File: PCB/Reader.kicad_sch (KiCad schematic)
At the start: 42 parts, among them J1 Conn_01x04, J2 Amphenol Dubox ‎76383-402LF‎, J3 Conn_01x04, J4 Conn_01x08, J5 Conn_01x10, J6 Conn_01x03, J7 Conn_01x02, Q1 2N7002, Q2 2N7002, Q3 2N7002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

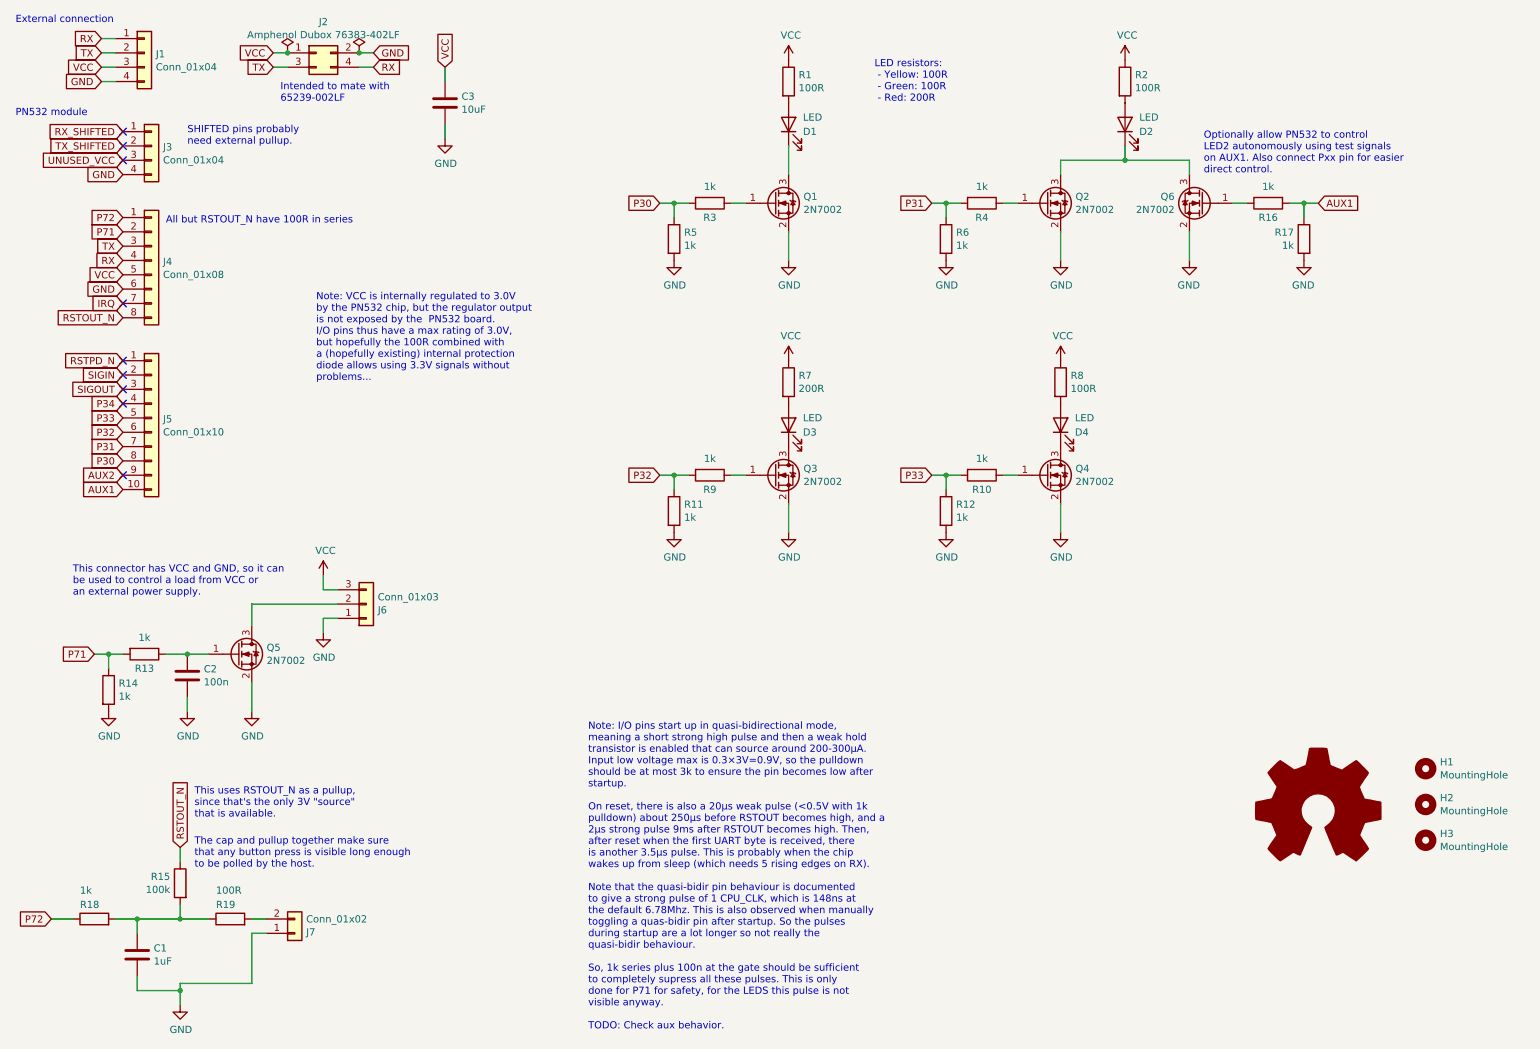
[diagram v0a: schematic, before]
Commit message: Improve some schematic notes
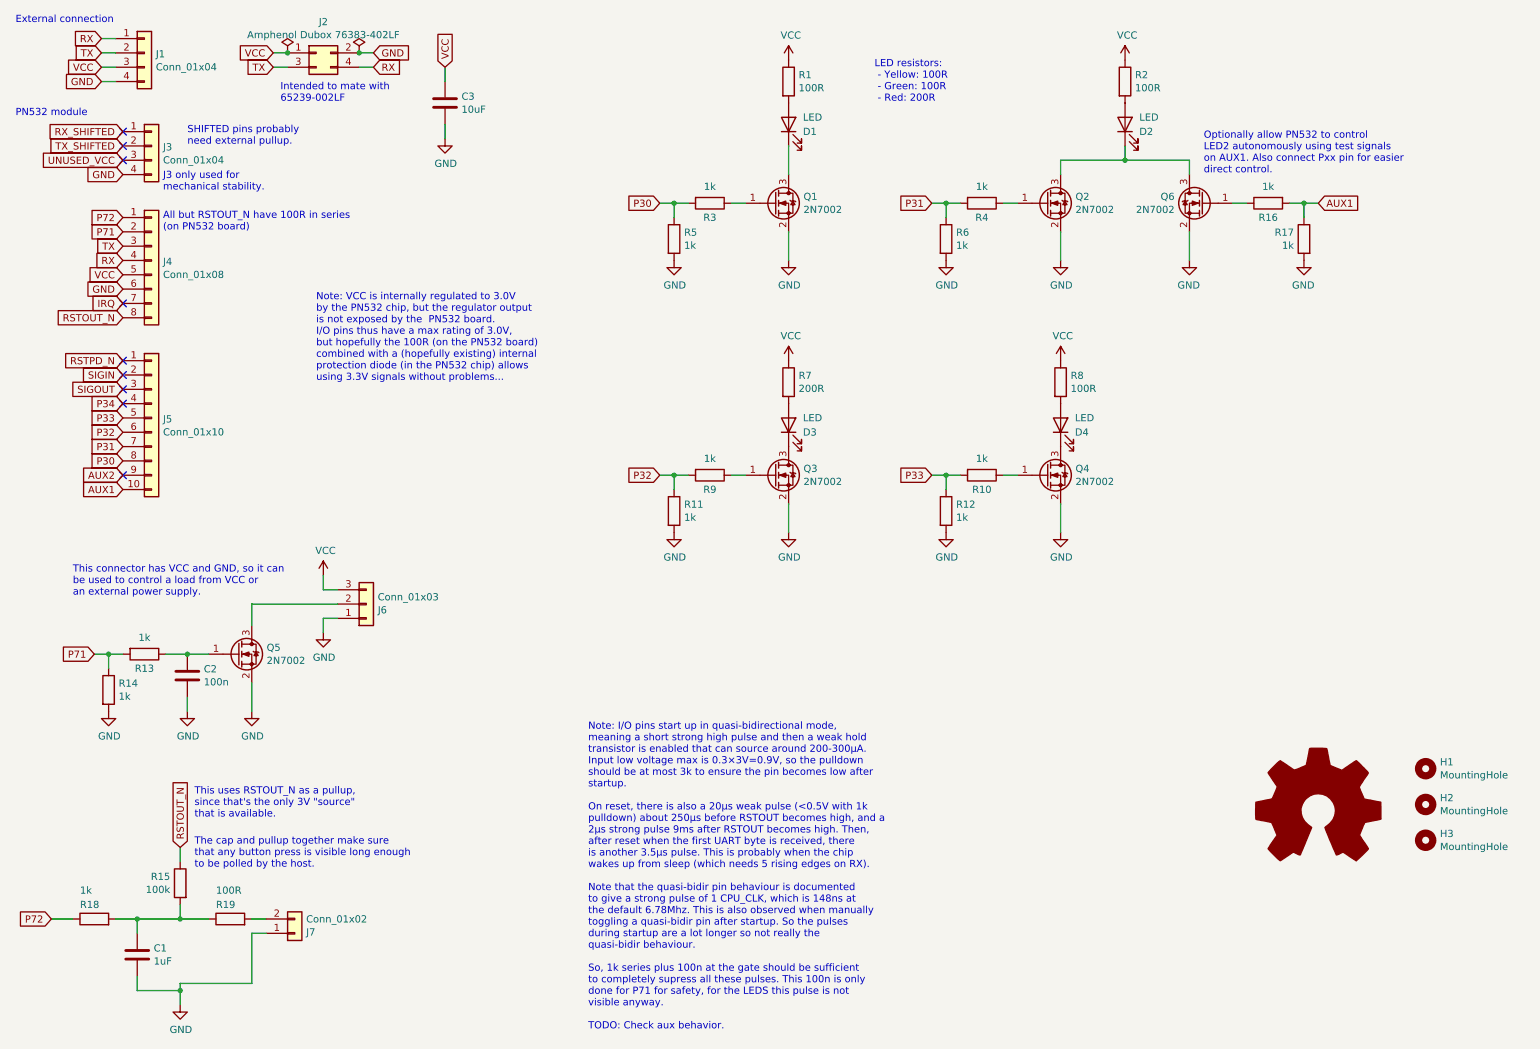
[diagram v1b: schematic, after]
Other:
- note added: "All but RSTOUT_N have 100R in series (on PN532 board)"
- note added: "J3 only used for mechanical stability."
- note added: "Note: VCC is internally regulated to 3.0V by the PN532 chip, but the regulator output is not exposed by the PN532 board. I/O pins thus have a max rating of 3.0V, but hopefully the 100R (on the PN532 board) combined with a (hopefully existing) internal protection diode (in the PN532 chip) allows using 3.3V signals without problems..."
- note removed: "All but RSTOUT_N have 100R in series"
- note removed: "Note: VCC is internally regulated to 3.0V by the PN532 chip, but the regulator output is not exposed by the PN532 board. I/O pins thus have a max rating of 3.0V, but hopefully the 100R combined with a (hopefully existing) internal protection diode allows using 3.3V signals without problems..."
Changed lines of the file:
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@@
 		)
 	)
-	(text "Note: VCC is internally regulated to 3.0V\nby the PN532 chip, but the regulator output\nis not exposed by the  PN532 board.\nI/O pins thus have a max rating of 3.0V,\nbut hopefully the 100R combined with\na (hopefully existing) internal protection\ndiode allows using 3.3V signals without\nproblems..."
+	(text "Note: VCC is internally regulated to 3.0V\nby the PN532 chip, but the regulator output\nis not exposed by the  PN532 board.\nI/O pins thus have a max rating of 3.0V,\nbut hopefully the 100R (on the PN532 board)\ncombined with a (hopefully existing) internal\nprotection diode (in the PN532 chip) allows\nusing 3.3V signals without problems..."
 		(exclude_from_sim no)
 		(at 68.58 78.74 0)
@@
 		)
 	)
-	(text "Note: I/O pins start up in quasi-bidirectional mode,\nmeaning a short strong high pulse and then a weak hold\ntransistor is enabled that can source around 200-300μA.\nInput low voltage max is 0.3×3V=0.9V, so the pulldown\nshould be at most 3k to ensure the pin becomes low after\nstartup.\n\nOn reset, there is also a 20μs weak pulse (<0.5V with 1k\npulldown) about 250μs before RSTOUT becomes high, and a\n2μs strong pulse 9ms after RSTOUT becomes high. Then,\nafter reset when the first UART byte is received, there\nis another 3.5μs pulse. This is probably when the chip\nwakes up from sleep (which needs 5 rising edges on RX).\n\nNote that the quasi-bidir pin behaviour is documented\nto give a strong pulse of 1 CPU_CLK, which is 148ns at\nthe default 6.78Mhz. This is also observed when manually\ntoggling a quas-bidir pin after startup. So the pulses\nduring startup are a lot longer so not really the\nquasi-bidir behaviour.\n\nSo, 1k series plus 100n at the gate should be sufficient\nto completely supress all these pulses. This is only\ndone for P71 for safety, for the LEDS this pulse is not\nvisible anyway.\n\nTODO: Check aux behavior."
+	(text "Note: I/O pins start up in quasi-bidirectional mode,\nmeaning a short strong high pulse and then a weak hold\ntransistor is enabled that can source around 200-300μA.\nInput low voltage max is 0.3×3V=0.9V, so the pulldown\nshould be at most 3k to ensure the pin becomes low after\nstartup.\n\nOn reset, there is also a 20μs weak pulse (<0.5V with 1k\npulldown) about 250μs before RSTOUT becomes high, and a\n2μs strong pulse 9ms after RSTOUT becomes high. Then,\nafter reset when the first UART byte is received, there\nis another 3.5μs pulse. This is probably when the chip\nwakes up from sleep (which needs 5 rising edges on RX).\n\nNote that the quasi-bidir pin behaviour is documented\nto give a strong pulse of 1 CPU_CLK, which is 148ns at\nthe default 6.78Mhz. This is also observed when manually\ntoggling a quasi-bidir pin after startup. So the pulses\nduring startup are a lot longer so not really the\nquasi-bidir behaviour.\n\nSo, 1k series plus 100n at the gate should be sufficient\nto completely supress all these pulses. This 100n is only\ndone for P71 for safety, for the LEDS this pulse is not\nvisible anyway.\n\nTODO: Check aux behavior."
 		(exclude_from_sim no)
 		(at 116.84 193.802 0)
+		(effects
+			(font
+				(size 1.27 1.27)
+			)
+			(justify left bottom)
+		)
+	)
+	(text "J3 only used for\nmechanical stability."
+		(exclude_from_sim no)
+		(at 41.402 44.958 0)
 		(effects
 			(font
@@
 		)
 	)
-	(text "All but RSTOUT_N have 100R in series"
+	(text "All but RSTOUT_N have 100R in series\n(on PN532 board)"
 		(exclude_from_sim no)
-		(at 41.91 50.8 0)
+		(at 41.402 48.514 0)
 		(effects
 			(font
 				(size 1.27 1.27)
 			)
-			(justify left bottom)
+			(justify left top)
 		)
 	)

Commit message: Improve revision silk and re-add OSHW logo
The logo got removed at some point, so re-add it.

Remove the PCB name on the front in favor of the silk on the back where
there is more room.

Match the PCB name to the git repo name, and auto-fill the board
revision.
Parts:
- added LOGO1: Logo_Open_Hardware_Large, Symbol:OSHW-Symbol_8.9x8mm_SilkScreen, symbol Graphic:Logo_Open_Hardware_Large
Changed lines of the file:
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@@
 		(unit 1)
 		(exclude_from_sim yes)
-		(in_bom yes)
+		(in_bom no)
 		(on_board yes)
 		(dnp no)
-		(property "Reference" "#LOGO1"
+		(property "Reference" "LOGO1"
 			(at 246.38 142.24 0)
 			(effects
@@
 			)
 		)
-		(property "Footprint" "Symbol:OSHW-Symbol_44.5x40mm_SilkScreen"
+		(property "Footprint" "Symbol:OSHW-Symbol_8.9x8mm_SilkScreen"
 			(at 246.38 154.94 0)
 			(effects
@@
 			(project "Reader"
 				(path "/f5709391-a389-450b-a647-2f06b3cb0d95"
-					(reference "#LOGO1")
+					(reference "LOGO1")
 					(unit 1)
 				)
